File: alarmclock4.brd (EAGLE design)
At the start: 60 x 92 mm, 37 parts, among them X1 MKDSN1,5/2-5,08, X2 MKDSN1,5/2-5,08, X3 MKDSN1,5/2-5,08, X4 MKDSN1,5/2-5,08

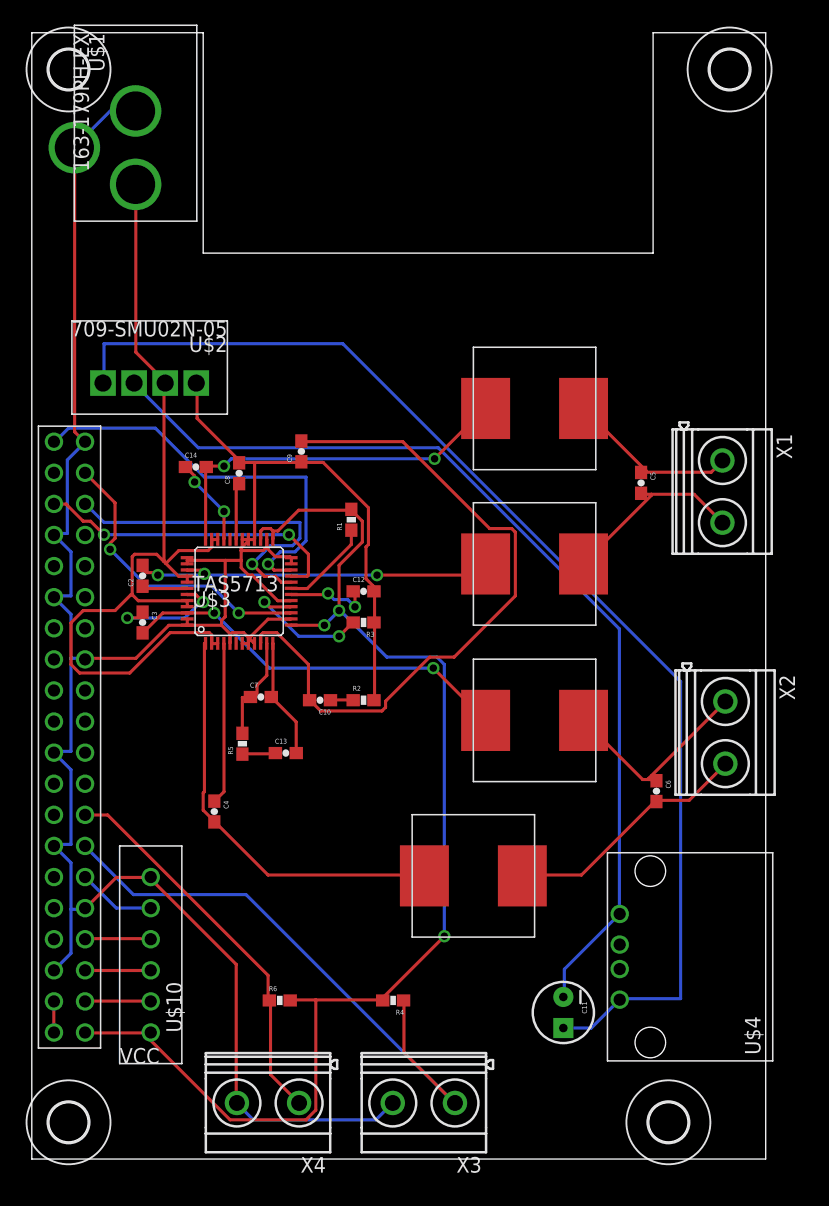
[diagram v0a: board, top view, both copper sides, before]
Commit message: - 2 bugfix: orientation of dc-dc + TAS pin SEL must not be to ground - remove via under the TAS chip
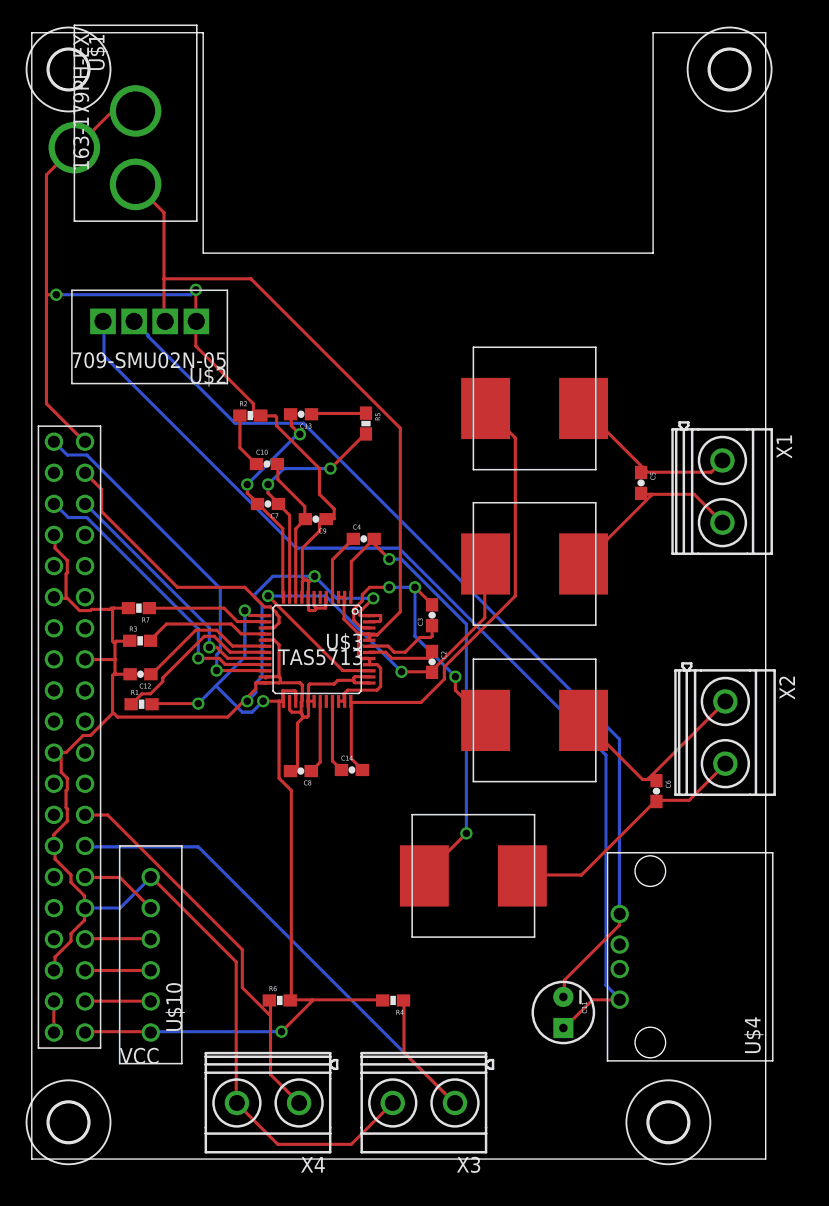
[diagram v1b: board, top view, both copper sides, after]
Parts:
- added R7: 15k, SparkFun-Passives:0603-RES
- moved R5 28.0 mm to (27.3, 60.1), turned to 270 degrees
- moved C14 27.8 mm to (26.1, 31.8)
- moved C13 27.7 mm to (22.0, 60.8), turned to 180 degrees
- moved C4 25.4 mm to (27.1, 50.7), turned to 0 degrees
- moved R2 25.0 mm to (17.9, 60.7)
- moved C8 24.8 mm to (22.0, 31.7), turned to 180 degrees
- moved C2 24.7 mm to (32.7, 40.6), turned to 270 degrees
- moved C3 23.7 mm to (32.7, 44.4), turned to 90 degrees
- moved R1 22.8 mm to (8.97, 37.1), turned to 0 degrees
- moved C10 19.8 mm to (19.2, 56.8), turned to 0 degrees
- moved C12 19.4 mm to (8.88, 39.6), turned to 180 degrees
- moved R3 18.3 mm to (8.85, 42.3), turned to 0 degrees
- moved C7 15.8 mm to (19.3, 53.5), turned to 180 degrees
- moved U$3 7.94 mm to (23.3, 41.6), turned to 180 degrees
- moved C9 5.65 mm to (23.2, 52.3), turned to 180 degrees
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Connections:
- new net N$34: R7.1, U$3.P$14
- net GND: now also R7.2; no longer U$3.P$14
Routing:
- net N$23: track 55.8 -> 12.2 mm
- net GND: track 216.4 -> 249.8 mm, vias 0 -> 5
- net +3V3: track 103.2 -> 76.6 mm, vias 3 -> 4
- net N$3: track 98.3 -> 83.4 mm
- net N$21: track 8.85 -> 19.6 mm, vias 0 -> 2
- net N$34: track 0.00 -> 9.92 mm
- net N$10: track 30.7 -> 39.9 mm, vias 2 -> 0
- net N$14: track 32.3 -> 23.7 mm, vias 2 -> 3
- net N$22: track 9.86 -> 18.4 mm, vias 0 -> 2
- net N$12: track 13.2 -> 5.48 mm
- net N$4: track 28.1 -> 20.9 mm
- net N$28: track 7.58 -> 13.9 mm
- net N$16: track 31.2 -> 37.5 mm, vias 3 -> 2
- net VCC: track 75.2 -> 70.5 mm
- net N$1: track 33.9 -> 29.3 mm
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
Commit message: move the capa
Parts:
- moved C11 3.58 mm to (40.2, 13.5)
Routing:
- net N$13: track 38.3 -> 70.6 mm, vias 2 -> 0
- net N$14: track 23.7 -> 35.7 mm
- net N$21: track 19.6 -> 30.7 mm
- net GND: track 249.8 -> 239.2 mm, vias 5 -> 1
- net N$17: track 5.91 -> 15.7 mm
- net N$22: track 18.4 -> 25.0 mm
- net +3V3: track 76.6 -> 82.5 mm, vias 4 -> 5
- net N$2: track 23.6 -> 20.0 mm, vias 0 -> 2
- net N$1: track 29.3 -> 33.0 mm
- net N$3: track 83.4 -> 87.0 mm
- net N$4: track 20.9 -> 23.8 mm
- net N$15: track 6.76 -> 9.62 mm, vias 0 -> 2
- net N$16: track 37.5 -> 34.7 mm
- net N$10: track 39.9 -> 41.2 mm, vias 0 -> 2
- net N$28: track 13.9 -> 12.7 mm
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
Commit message: recompute
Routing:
- net N$13: track 70.6 -> 32.9 mm, vias 0 -> 2
- net N$16: track 34.7 -> 16.7 mm, vias 2 -> 0
- net N$21: track 30.7 -> 17.1 mm
- net GND: track 239.2 -> 228.2 mm, vias 1 -> 2
- net N$17: track 15.7 -> 5.17 mm
- net VCC: track 71.1 -> 79.6 mm, vias 2 -> 3
- net N$22: track 25.0 -> 18.1 mm
- net +3V3: track 82.5 -> 75.9 mm, vias 5 -> 3
- net N$4: track 23.8 -> 27.6 mm
- net N$2: track 20.0 -> 23.2 mm, vias 2 -> 1
- net N$15: track 9.62 -> 7.08 mm
- net N$1: track 33.0 -> 31.7 mm
- net N$10: track 41.2 -> 39.9 mm, vias 2 -> 0
- net N$6: track 31.9 -> 33.1 mm

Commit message: recompute
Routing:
- net VCC: track 79.6 -> 56.4 mm, vias 3 -> 1
- net N$28: track 13.1 -> 34.4 mm, vias 0 -> 2
- net N$16: track 16.7 -> 34.9 mm, vias 0 -> 2
- net N$14: track 35.7 -> 22.6 mm, vias 3 -> 2
- net GND: track 228.2 -> 234.1 mm, vias 2 -> 3
- net N$4: track 27.6 -> 22.8 mm
- net N$5: track 23.1 -> 27.1 mm
- net +3V3: track 75.9 -> 79.0 mm
- net N$15: track 7.08 -> 5.84 mm, vias 2 -> 0
- net N$22: track 18.1 -> 17.0 mm
